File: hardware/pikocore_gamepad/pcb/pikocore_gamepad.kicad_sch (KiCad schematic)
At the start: 0 parts

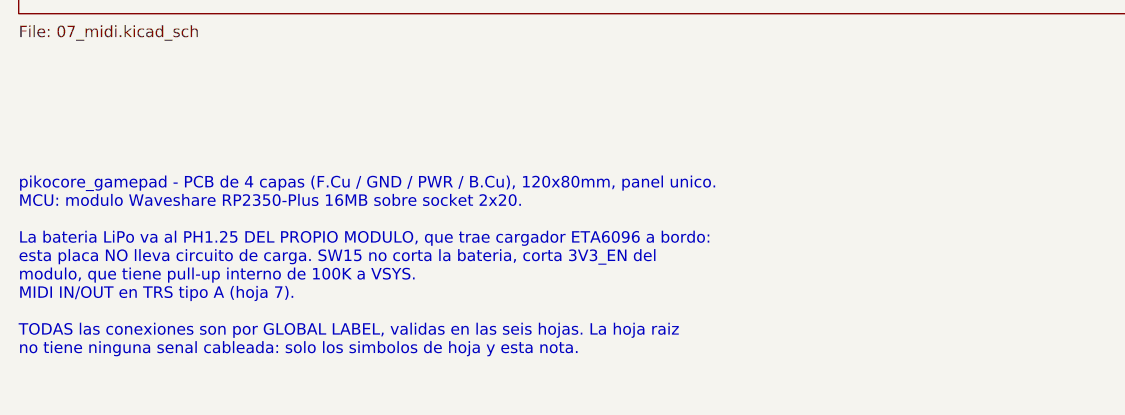
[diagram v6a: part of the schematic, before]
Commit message: hw: U1 soldado plano en la descripcion, nota raiz a 100x60 y .gitattributes
- netlist.py/gen_sch.py: U1 y la nota raiz ya no dicen "socket 2x20"; la nota
  dice 100x60, no afirma el modelo del conector de bateria y el MIDI va en su
  propio parrafo. Esquematico y .net regenerados; la placa no cambia (su U1
  tiene Description vacia) y se re-guardo por pcbnew byte a byte igual.
- check_placement.py: el comentario de via contra pastilla de U1 aclara que
  la prueba con el rectangulo envolvente es conservadora (pastillas estadio).
- .gitattributes: *.sh con eol=lf (route_cycle.sh no corre con CRLF).

Co-Authored-By: Claude Opus 5.5 <noreply@anthropic.com>
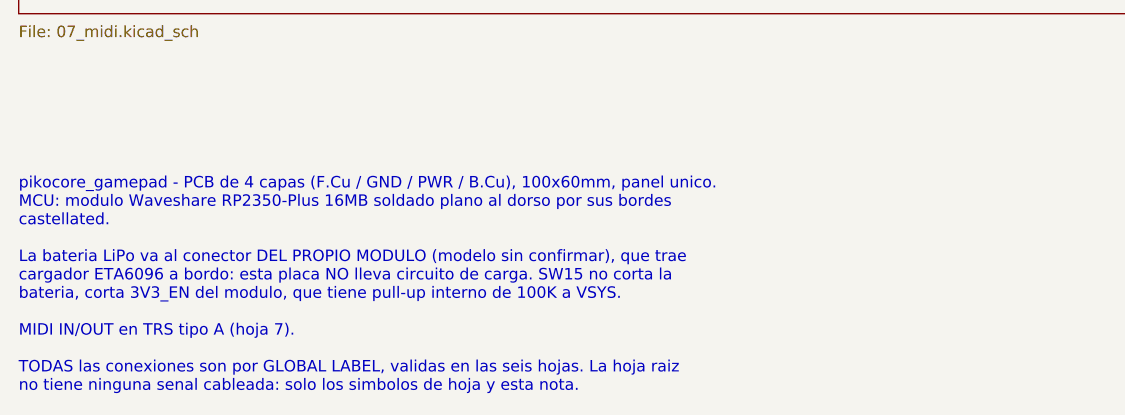
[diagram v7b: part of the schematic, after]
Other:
- note added: "pikocore_gamepad - PCB de 4 capas (F.Cu / GND / PWR / B.Cu), 100x60mm, panel unico. MCU: modulo Waveshare RP2350-Plus 16MB soldado plano al dorso por sus bordes castellated. La bateria LiPo va al conector DEL PROPIO MODULO (modelo sin confirmar), que trae cargador ETA6096 a bordo: esta placa NO lleva circuito de carga. SW15 no corta la bateria, corta 3V3_EN del modulo, que tiene pull-up interno d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"
- note removed: "pikocore_gamepad - PCB de 4 capas (F.Cu / GND / PWR / B.Cu), 120x80mm, panel unico. MCU: modulo Waveshare RP2350-Plus 16MB sobre socket 2x20. La bateria LiPo va al PH1.25 DEL PROPIO MODULO, que trae cargador ETA6096 a bordo: esta placa NO lleva circuito de carga. SW15 no corta la bateria, corta 3V3_EN del modulo, que tiene pull-up interno de 100K a VSYS. MIDI IN/OUT en TRS tipo A (hoja 7). TODAS 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"
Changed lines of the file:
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@@
     (date "2026-08-28")
     (rev "A")
-    (comment 1 "MCU: Waveshare RP2350-Plus 16MB en socket | LiPo al PH1.25 del modulo")
+    (comment 1 "MCU: Waveshare RP2350-Plus 16MB soldado plano | LiPo al conector del modulo")
     (comment 2 "Pinout: pinmap.py, verificado contra el firmware por la puerta G-4")
   )
@@
     (effects (font (size 1.27 1.27)) (justify left top))
   )
-  (text "pikocore_gamepad - PCB de 4 capas (F.Cu / GND / PWR / B.Cu), 120x80mm, panel unico.\nMCU: modulo Waveshare RP2350-Plus 16MB sobre socket 2x20.\n\nLa bateria LiPo va al PH1.25 DEL PROPIO MODULO, que trae cargador ETA6096 a bordo:\nesta placa NO lleva circuito de carga. SW15 no corta la bateria, corta 3V3_EN del\nmodulo, que tiene pull-up interno de 100K a VSYS.\nMIDI IN/OUT en TRS tipo A (hoja 7).\n\nTODAS las conexiones son por GLOBAL LABEL, validas en las seis hojas. La hoja raiz\nno tiene ninguna senal cableada: solo los simbolos de hoja y esta nota." (exclude_from_sim no) (at 30 211 0)
+  (text "pikocore_gamepad - PCB de 4 capas (F.Cu / GND / PWR / B.Cu), 100x60mm, panel unico.\nMCU: modulo Waveshare RP2350-Plus 16MB soldado plano al dorso por sus bordes\ncastellated.\n\nLa bateria LiPo va al conector DEL PROPIO MODULO (modelo sin confirmar), que trae\ncargador ETA6096 a bordo: esta placa NO lleva circuito de carga. SW15 no corta la\nbateria, corta 3V3_EN del modulo, que tiene pull-up interno de 100K a VSYS.\n\nMIDI IN/OUT en TRS tipo A (hoja 7).\n\nTODAS las conexiones son por GLOBAL LABEL, validas en las seis hojas. La hoja raiz\nno tiene ninguna senal cableada: solo los simbolos de hoja y esta nota." (exclude_from_sim no) (at 30 211 0)
     (effects (font (size 1.27 1.27)) (justify left top))
   )

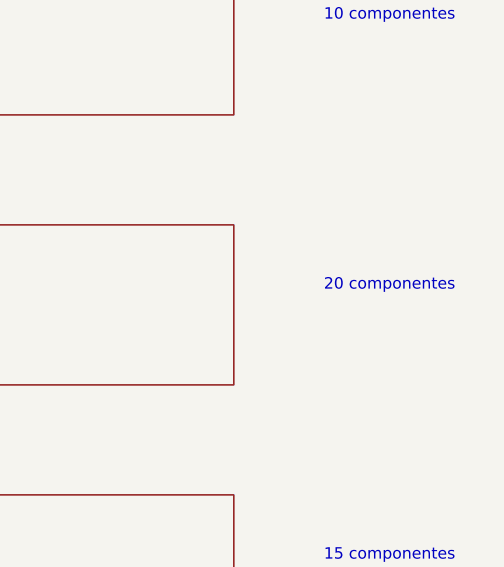
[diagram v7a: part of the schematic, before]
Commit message: hw: pantalla de 7 pines en el esquema (sin FPC, backlight ni TE)
J4 pasa a ser el modulo IPS 1.3in ST7789 de 7 pines pasantes (simbolo
LCD_ST7789, huella gamesetup_fp:LCD_ST7789_240x240_7P, MANUAL, sin LCSC):
pines 1..7 = GND, 3V3, LCD_SCK, LCD_MOSI, LCD_RES, LCD_DC, LCD_BLK. Fuera
LCD1, R21, Q1, R22, C30, C31, los simbolos LCD_FPC24/LCD_PANEL/Q_NMOS y el
27R (C17594) de LCSC_PASIVOS. CS a GND y el transistor del backlight van en
el modulo; nota de la hoja 02 actualizada.

GP26 queda libre (FREE = (26,)), sin PIN_LCD_TE en config.h. Los GPIO libres
van a no_connect en vez de una etiqueta EXP_GP* de un solo extremo.

params.py: fuera PANEL_* y LCD_FPC_PIN_ORDER; entran las cotas LCD7_* del
dibujo del fabricante (verificadas) salvo LCD7_PIN_ROW_TO_EDGE (1.27) y
LCD7_PIN_DRILL (1.0), que se miden con el modulo en mano. gen_fp.py lleva la
geometria del modulo; la escritura de la huella y la colocacion son la
siguiente tarea (dos tests de footprint quedan rojos hasta entonces).

Co-Authored-By: Claude Sonnet 5.5 <noreply@anthropic.com>
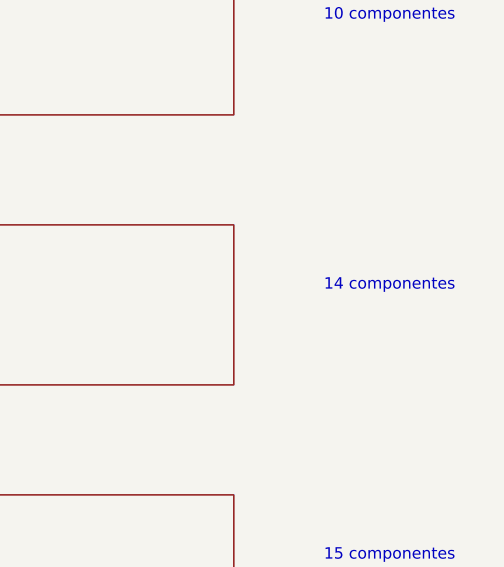
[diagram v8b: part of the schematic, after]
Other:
- note removed: "20 componentes"
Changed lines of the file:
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@@
     )
   )
-  (text "20 componentes" (exclude_from_sim no) (at 205 61 0)
+  (text "14 componentes" (exclude_from_sim no) (at 205 61 0)
     (effects (font (size 1.27 1.27)) (justify left top))
   )
